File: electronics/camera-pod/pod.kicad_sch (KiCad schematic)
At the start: 16 parts, among them J1 LEAD, J2 MEGA, U1 AMS1117-3.3

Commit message: Camera pod: the PCBA review's fixes
P1: the LED resistors are 100 Ohm 0805 (C17408, a basic part; no 82 Ohm
exists as a basic 0805 or 1206).  Over the LEDs' Vf spread at that
current (about 2.65-3.2 V) and CAM_5V at 5.0-5.2 V that gives 18-26 mA
per LED, at most 66 mW in a 125 mW resistor and 102 mA for the four,
inside the node's camera budget.  56 Ohm 0603 gave 36-44 mA and up to
108 mW in 100 mW.  The light drops by about a third from the 32 mA
first planned, about 0.6 EV, which the Mega's auto-exposure takes.
P2: the AMS1117's ringing on its 22 uF MLCC is on the bring-up list,
with the LED current.  P3: a CAM_5V load switch on IO5/IO6 noted for a
later node.

The CPL audit agrees on all 14 parts.  ERC 0, DRC 0, parity 0, 0
unconnected; the BOM follows.

Co-Authored-By: Claude Opus 5.5 <noreply@anthropic.com>
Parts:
- R1, R2, R3, R4: value 56 -> 100; footprint Resistor_SMD:R_0603_1608Metric -> Resistor_SMD:R_0805_2012Metric; LCSC C25196 -> C17408; MPN 0603WAF560JT5E -> 0805W8F1000T5E
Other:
- note added: "Light: four white LEDs, 100 Ω each from CAM_5V, cathodes to LED_K (the node's low side)"
- note removed: "Light: four white LEDs, 56 Ω each from CAM_5V, cathodes to LED_K (the node's low side)"
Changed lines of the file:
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@@
 		)
 	)
-	(text "Light: four white LEDs, 56 Ω each from CAM_5V, cathodes to LED_K (the node's low side)"
+	(text "Light: four white LEDs, 100 Ω each from CAM_5V, cathodes to LED_K (the node's low side)"
 		(exclude_from_sim no)
 		(at 20.32 133.35 0)
@@
 			)
 		)
-		(property "Value" "56"
+		(property "Value" "100"
 			(at 93.98 62.23 0)
 			(effects
@@
 			)
 		)
-		(property "Footprint" "Resistor_SMD:R_0603_1608Metric"
+		(property "Footprint" "Resistor_SMD:R_0805_2012Metric"
 			(at 91.44 64.77 0)
 			(effects
@@
 			)
 		)
-		(property "Description" "Resistor 56 0603"
+		(property "Description" "Resistor 100 0805"
 			(at 91.44 64.77 0)
 			(effects
@@
 			)
 		)
-		(property "LCSC" "C25196"
+		(property "LCSC" "C17408"
 			(at 91.44 64.77 0)
 			(effects
@@
 			)
 		)
-		(property "MPN" "0603WAF560JT5E"
+		(property "MPN" "0805W8F1000T5E"
 			(at 91.44 64.77 0)
 			(effects
@@
 			)
 		)
-		(property "Value" "56"
+		(property "Value" "100"
 			(at 83.82 62.23 0)
 			(effects
@@
 			)
 		)
-		(property "Footprint" "Resistor_SMD:R_0603_1608Metric"
+		(property "Footprint" "Resistor_SMD:R_0805_2012Metric"
 			(at 81.28 64.77 0)
 			(effects
@@
 			)
 		)
-		(property "Description" "Resistor 56 0603"
+		(property "Description" "Resistor 100 0805"
 			(at 81.28 64.77 0)
 			(effects
@@
 			)
 		)
-		(property "LCSC" "C25196"
+		(property "LCSC" "C17408"
 			(at 81.28 64.77 0)
 			(effects
@@
 			)
 		)
-		(property "MPN" "0603WAF560JT5E"
+		(property "MPN" "0805W8F1000T5E"
 			(at 81.28 64.77 0)
 			(effects
@@
 			)
 		)
-		(property "Value" "56"
+		(property "Value" "100"
 			(at 73.66 62.23 0)
 			(effects
@@
 			)
 		)
-		(property "Footprint" "Resistor_SMD:R_0603_1608Metric"
+		(property "Footprint" "Resistor_SMD:R_0805_2012Metric"
 			(at 71.12 64.77 0)
 			(effects
@@
 			)
 		)
-		(property "Description" "Resistor 56 0603"
+		(property "Description" "Resistor 100 0805"
 			(at 71.12 64.77 0)
 			(effects
@@
 			)
 		)
-		(property "LCSC" "C25196"
+		(property "LCSC" "C17408"
 			(at 71.12 64.77 0)
 			(effects
@@
 			)
 		)
-		(property "MPN" "0603WAF560JT5E"
+		(property "MPN" "0805W8F1000T5E"
 			(at 71.12 64.77 0)
 			(effects
@@
 			)
 		)
-		(property "Value" "56"
+		(property "Value" "100"
 			(at 63.5 62.23 0)
 			(effects
@@
 			)
 		)
-		(property "Footprint" "Resistor_SMD:R_0603_1608Metric"
+		(property "Footprint" "Resistor_SMD:R_0805_2012Metric"
 			(at 60.96 64.77 0)
 			(effects
@@
 			)
 		)
-		(property "Description" "Resistor 56 0603"
+		(property "Description" "Resistor 100 0805"
 			(at 60.96 64.77 0)
 			(effects
@@
 			)
 		)
-		(property "LCSC" "C25196"
+		(property "LCSC" "C17408"
 			(at 60.96 64.77 0)
 			(effects
@@
 			)
 		)
-		(property "MPN" "0603WAF560JT5E"
+		(property "MPN" "0805W8F1000T5E"
 			(at 60.96 64.77 0)
 			(effects
@@
 		)
 	)
-	(text_box "J1 is the bay node's J6 mirrored: a 'Same direction' PH 8 lead (pin n to pin 9−n) joins them.\nJ2 follows the Mega's own pin order; the names are on the silkscreen, its cable plugs on by name.\nThe Mega from 3.3 V (U1, ≈ 0.2 W at 120 mA): its MISO is 3.3 V.  LEDs ≈ 32 mA each (Vf ≈ 3.2 V), 128 mA,\n  off unless the node's AO3400A pulls LED_K low (PWM ≥ 20 kHz or on/off).  CAM_5V: the node's 0.5 A PTC."
+	(text_box "J1 is the bay node's J6 mirrored: a 'Same direction' PH 8 lead (pin n to pin 9−n) joins them.\nJ2 follows the Mega's own pin order; the names are on the silkscreen, its cable plugs on by name.\nThe Mega from 3.3 V (U1, ≈ 0.2 W at 120 mA): its MISO is 3.3 V.  LEDs 18–26 mA each (100 Ω 0805, ≤ 66 mW),\n  ≤ 102 mA for the four, off unless the node's AO3400A pulls LED_K low (PWM ≥ 20 kHz or on/off).\nCAM_5V: the node's 0.5 A PTC, no switch: a hung camera (the Mega has no reset pin) needs a power cycle."
 		(exclude_from_sim no)
 		(at 20.32 165.1 0)
-		(size 240.03 13.97)
+		(size 240.03 16.51)
 		(margins 1.5 1.5 1.5 1.5)
 		(stroke

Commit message: Schematic review S1, S4, S6: POS_IN 150k, the hub's ON LEDs on 18k, the camera's 0.75 A PTC
The user approved them ("S1 oui / S6 oui / S4 oui").

* S1, bay node: R29 470k -> 150k (C22807, basic).
  - Before its firmware runs, the upstream POS output (a node's IO42, the
    hub's IO10-13) floats. The BAT54S's warm leakage (about 2-3 uA at
    65 C) could then lift POS_IN through 470k to VIL.
  - Driven high through R30 + R28, 150k still gives 2.87 V, above VIH.
  - The design.py notes and bay_node.dtsi follow.
* S4, power hub: R41-R44 (the ON LEDs on the row outputs) 10k -> 18k
  (C25810, already on the board): 1.4 mA and 37 mW at 28 V. The 10k
  ran at 75 % of its 0603 rating at 29.4 V.
* S6, bay node: F1 (CAM_5V) goes from the 0.5 A PTC to SMD1206P075TF
  (RUILON, C20987, new catalog key pptc750): 0.75 A hold, 1.5 A trip,
  the same 1206 footprint. It is extended like C20799, so no fee changes.
  - Arducam gives the Mega 317 mA working: with the LEDs that is
    ~0.42 A on CAM_5V, where the 0.5 A part holds ~0.31 A at 70 C.
  - The camera pod's LDO tab gets the copper its routing leaves: a
    top-side +3V3 pour round the tab and a bottom-side island, joined by
    three vias. U1 drops ~0.5 W at 317 mA. The routing is unchanged.
  - The "~120 mA" notes go to 317 mA (node and pod design.py,
    electronics.md).
  - The bay's worst case follows: <= 2.25 A on +5V, the buck's inductor
    peaking at ~2.65 A (under its 2.9 A minimum limit), 13.5 W from
    VRACK (power-distribution-review.md, the buck notes).

The routed PCBs keep their routing.
- Node and hub: only the changed parts' properties (KiCad's Python, as
  pcbgen sets them).
- Pod: the two new zones and three vias, refilled.
- ERC 0, DRC 0, unconnected 0, parity 0 on all three (run on the Mac:
  zephyrbox didn't answer).
- keep_unchanged kept the node's renders and the hub's Gerbers. The
  hub's bottom render is restored: 9 pixels of via-hole noise, as before.
- The pod's renders, Gerbers and viewer GLB chang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
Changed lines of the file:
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@@
 		)
 	)
-	(text_box "J1 is the bay node's J6 mirrored: a 'Same direction' PH 8 lead (pin n to pin 9−n) joins them.\nJ2 follows the Mega's own pin order; the names are on the silkscreen, its cable plugs on by name.\nThe Mega from 3.3 V (U1, ≈ 0.2 W at 120 mA): its MISO is 3.3 V.  LEDs 18–26 mA each (100 Ω 0805, ≤ 66 mW),\n  ≤ 102 mA for the four, off unless the node's AO3400A pulls LED_K low (PWM ≥ 20 kHz or on/off).\nCAM_5V: the node's 0.5 A PTC, no switch: a hung camera (the Mega has no reset pin) needs a power cycle."
+	(text_box "J1 is the bay node's J6 mirrored: a 'Same direction' PH 8 lead (pin n to pin 9−n) joins them.\nJ2 follows the Mega's own pin order; the names are on the silkscreen, its cable plugs on by name.\nThe Mega from 3.3 V (U1, ≈ 0.5 W at its 317 mA max, Arducam): its MISO is 3.3 V.  LEDs 18–26 mA each (100 Ω 0805, ≤ 66 mW),\n  ≤ 102 mA for the four, off unless the node's AO3400A pulls LED_K low (PWM ≥ 20 kHz or on/off).\nCAM_5V: the node's 0.75 A PTC, no switch: a hung camera (the Mega has no reset pin) needs a power cycle."
 		(exclude_from_sim no)
 		(at 20.32 165.1 0)

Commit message: Datasheet audit F1-F6: the pod's AP2114H, STB 5.1k, PC_DET hysteresis, the camera ESD's 100 nF, the eFuse step
The user approved the audit's fixes for the node, the hub and the pod
("Go pour 1"); docs/datasheet-audit.md marks F1-F6 applied.

* F1, camera pod: U1 AMS1117-3.3 -> AP2114H-3.3TRG1 (C150716, catalog
  ldo_1a, the node's U2).
  - The AMS1117 is specified stable only with 22 uF tantalum; the
    AP2114H is stable with the ceramic C2.
  - Same SOT-223 pinout, copper (the +3V3 pour and island round the
    tab stay) and 180 deg CPL correction.
  - One more extended type on the pod's Economic order: +$3.09 and
    $0.05 of parts (JLC_SINCE_QUOTE).
* F2, power hub: R214 (TJA1462 STB pull-down) 10k -> 5.1k (C23186,
  already on the board). With IO9 floating, STB's internal pull-up
  (20 kOhm minimum) left it at up to 1.10 V, over VIL 0.99 V.
* F3, bay node: R42 150k from MUX_SEL back to PC_DET, beside U7 (C22807,
  on the board since S1).
  - The laptop's VBUS rises at ~50 us/V through R11/R12, where the
    LVC1G32 wants <= 10 ns/V and warns of oscillation.
  - This gives ~0.14 V of hysteresis.
* F4, bay node: C28 100 nF (C14663) on U12/U13's VBUS pins (+3V3), above
  U12 by its pin 5. Between the two ICs their courtyards leave no room.
* F5, node and hub: firmware.md's first-flash procedure gains the
  irreversible DIS_USB_OTG_DOWNLOAD_MODE eFuse step. In USB-OTG
  download boot the ROM drives IO40 high: the node's DUT_FLT_N, the
  hub's PD_SCL. Nothing is burnt.
* F6, notes, hub:
  - the IMON filter is 0.9 ms, not 47 us: the pin is a current source;
  - the buck stops at ~3.8 V (internal UVLO);
  - SHDN turns on at >= 1 V;
  - the soft start stays under the limit only typically;
  - the CH224A note follows CH224 V2.1: the source PDOs are listed for
    both parts and readable under 100 W, which is still to check with
    ours (review R3); single-byte transfers; no "same die".
* F6, notes, node: TPS2553D; the LDO's 1.94 V x 0.4 A ~ 0.8 W; L1's
  7.5 A guarante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
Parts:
- U1: value AMS1117-3.3 -> AP2114H-3.3TRG1; LCSC C6186 -> C150716; MPN AMS1117-3.3 -> AP2114H-3.3TRG1; Manufacturer AMS -> Diodes Incorporated
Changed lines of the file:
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@@
 			)
 		)
-		(property "Value" "AMS1117-3.3"
+		(property "Value" "AP2114H-3.3TRG1"
 			(at 76.2 109.22 0)
 			(effects
@@
 			)
 		)
-		(property "Datasheet" ""
+		(property "Datasheet" "https://www.diodes.com/assets/Datasheets/AP2114.pdf"
 			(at 76.2 100.33 0)
 			(effects
@@
 			)
 		)
-		(property "Description" "3.3 V 1 A LDO"
+		(property "Description" "3.3 V 1 A LDO, 450 mV dropout at 1 A, SOT-223"
 			(at 76.2 100.33 0)
 			(effects
@@
 			)
 		)
-		(property "MPN" "AMS1117-3.3"
+		(property "MPN" "AP2114H-3.3TRG1"
 			(at 76.2 100.33 0)
 			(effects
@@
 			)
 		)
-		(property "Manufacturer" "AMS"
+		(property "Manufacturer" "Diodes Incorporated"
 			(at 76.2 100.33 0)
 			(effects
@@
 			)
 		)
-		(property "LCSC" "C6186"
+		(property "LCSC" "C150716"
 			(at 76.2 100.33 0)
 			(effects

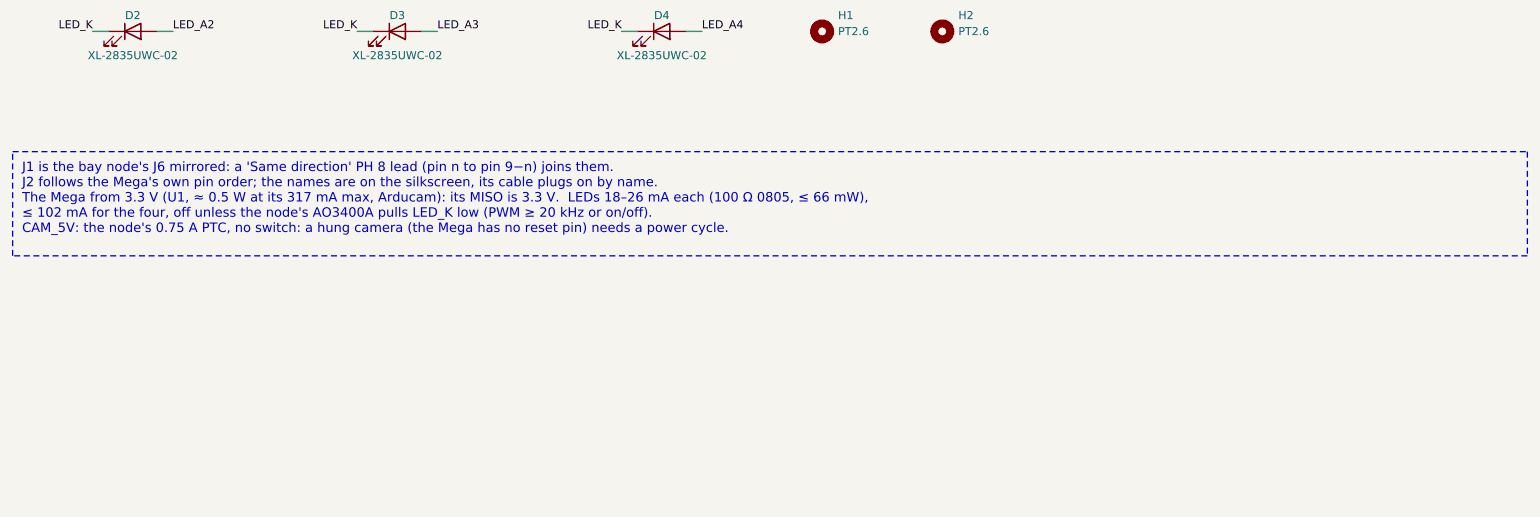
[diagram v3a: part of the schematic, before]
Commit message: Boards: labelled bottom test pads; hub dVdT 100 nF, 50 ms FLT blank
Eve's DFT rule on the four boards this session owns: bare pads on the
bottom, named on B.SilkS, out of the BOM and the CPL (no part, no
assembly fee).  Supply pads 1.5 mm, signal pads 1.0 mm (new catalog
entry "testpad1"), all more than 2 mm from any THT pad or hole
(closest: 4.7 mm, the pod's TP4).  Positions are fixed in design.py,
so they stay put across revisions.

- bay node, 17: TX, RX, 3V3, GND by the module (kept), then EN, IO0,
  FLT (DUT_FLT_N), ALRT (INA_ALERT_N), SDA, SCL and a second GND;
  a supply row along the bottom edge: GND, VIN, 5V, 3V3, DUT 5V,
  CAM 5V
- power hub, 20: TX, RX, 3V3, GND, 5V, VRACK, GND (kept), then EN,
  IO0, the CH224A's PD SDA/SCL, each row's FLT and IMON (A-D) and a
  third GND in the middle
- camera pod, 4: GND, 5V, 3V3 and a second GND at the far end
- DATA port, 2: GND and 5V (VBUS, through a via under its track)

Hub, as the datasheet audit's U1 answer asks (TPS2660 Fig. 55 at
85 C: 8-10 ms at 21 W fails the 47 nF worst start, 33 ms at 14 W
covers 100 nF): C21-C24 dVdT 47 nF -> 100 nF, so a row's soft start
is 16-22 ms and dissipates about 7-9 W typical, 14 W worst, for
19-24 ms; the firmware's HUB_ROW_FLT_BLANK_MS goes 25 -> 50 ms to
cover it (worst case 39 ms).  docs/power.md, the audit row and the
hub notes say so.

Routing fallout: J1's A12/B1 GND now leaves through one drawn 0.5 mm
via so the automatic fan-out can't cut the VRACK pour off A9/B4; the
pod's LDO tab zones are exclusive so tracks no longer split them.

All four rerouted, tidied and checked: ERC 0, DRC 0, unconnected 0,
parity 0.  Gerbers, renders, schematics, viewer GLBs, the JLC
snapshot lines and the rack BOM regenerated.

Co-Authored-By: Claude Opus 5.5 <noreply@anthropic.com>
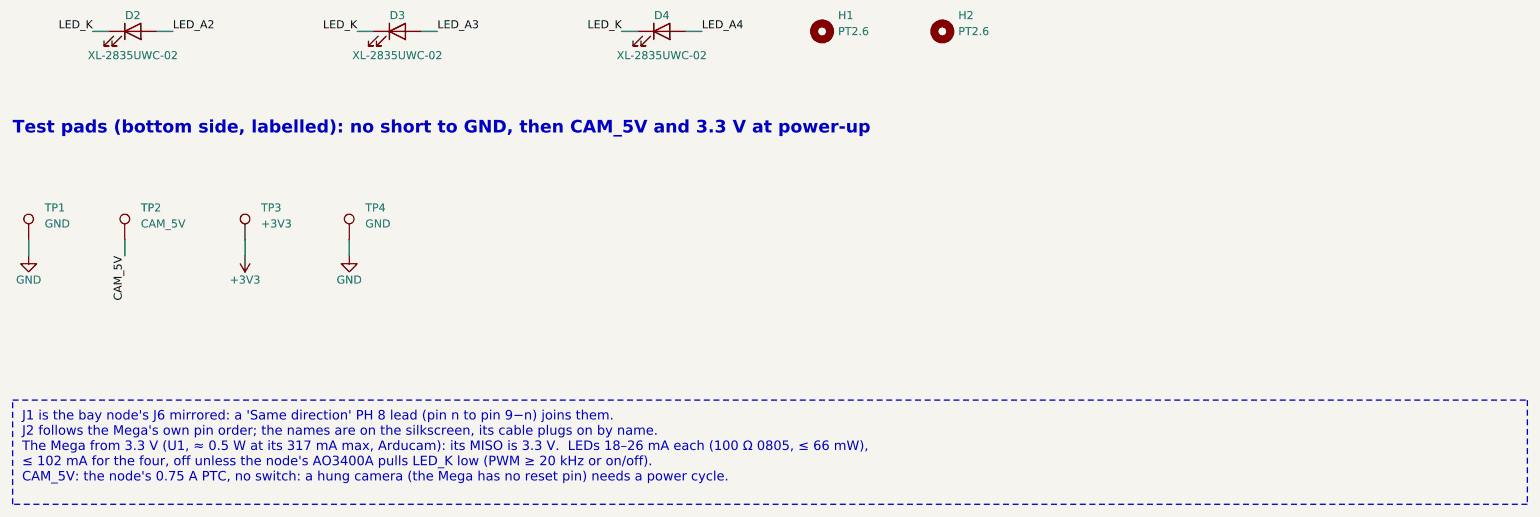
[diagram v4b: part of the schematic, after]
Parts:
- added TP1, TP4: GND, TestPoint:TestPoint_Pad_D1.5mm, symbol Connector:TestPoint
- added TP2: CAM_5V, TestPoint:TestPoint_Pad_D1.5mm, symbol Connector:TestPoint
- added TP3: +3V3, TestPoint:TestPoint_Pad_D1.5mm, symbol Connector:TestPoint
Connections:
- net +3V3: now also TP3.1
- net CAM_5V: now also TP2.1
- net GND: now also TP1.1, TP4.1
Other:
- note added: "Test pads (bottom side, labelled): no short to GND, then CAM_5V and 3.3 V at power-up"

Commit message: Camera pod: SPI and LED test pads by J1 (CP-3)
The kicad-happy review's CP-3, against Eve's rule: the pod had test
pads on its supplies only.  TP5-TP9 are bare 1.0 mm pads on B.Cu,
named on B.SilkS and kept out of the BOM and the CPL: SCK, MOSI, MISO,
CS and LED (LED_K, the LEDs' switched cathode).  They sit by J1, where
those lines come in from the node, and stay clear of the LDO's +3V3
island on B.Cu.  Each is on a new via drawn on its net's F.Cu track,
so no routing moves.  All are at least 2 mm from any through-hole pad
or hole and 2.6 mm from each other, and no label overlaps another.

Every track and via is main's.  The router added two things: a 4.5 mm
LED_K stub laid over the existing track to reach the new via, and a
40 um dot inside C1.1.  Same stitching.  ERC 0, DRC 0, unconnected 0,
parity 0.

Co-Authored-By: Claude Opus 5.5 <noreply@anthropic.com>
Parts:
- added TP5: SCK, TestPoint:TestPoint_Pad_D1.0mm, symbol Connector:TestPoint
- added TP6: MOSI, TestPoint:TestPoint_Pad_D1.0mm, symbol Connector:TestPoint
- added TP7: MISO, TestPoint:TestPoint_Pad_D1.0mm, symbol Connector:TestPoint
- added TP8: CS, TestPoint:TestPoint_Pad_D1.0mm, symbol Connector:TestPoint
- added TP9: LED_K, TestPoint:TestPoint_Pad_D1.0mm, symbol Connector:TestPoint
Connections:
- net CS: now also TP8.1
- net LED_K: now also TP9.1
- net MISO: now also TP7.1
- net MOSI: now also TP6.1
- net SCK: now also TP5.1
